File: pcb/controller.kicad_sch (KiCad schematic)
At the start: 3 parts, among them J1 Teensy 4.1 FEMALE 1x24, J2 Teensy 4.1 FEMALE 1x24, J3 VUSB from isolated Teensy pad

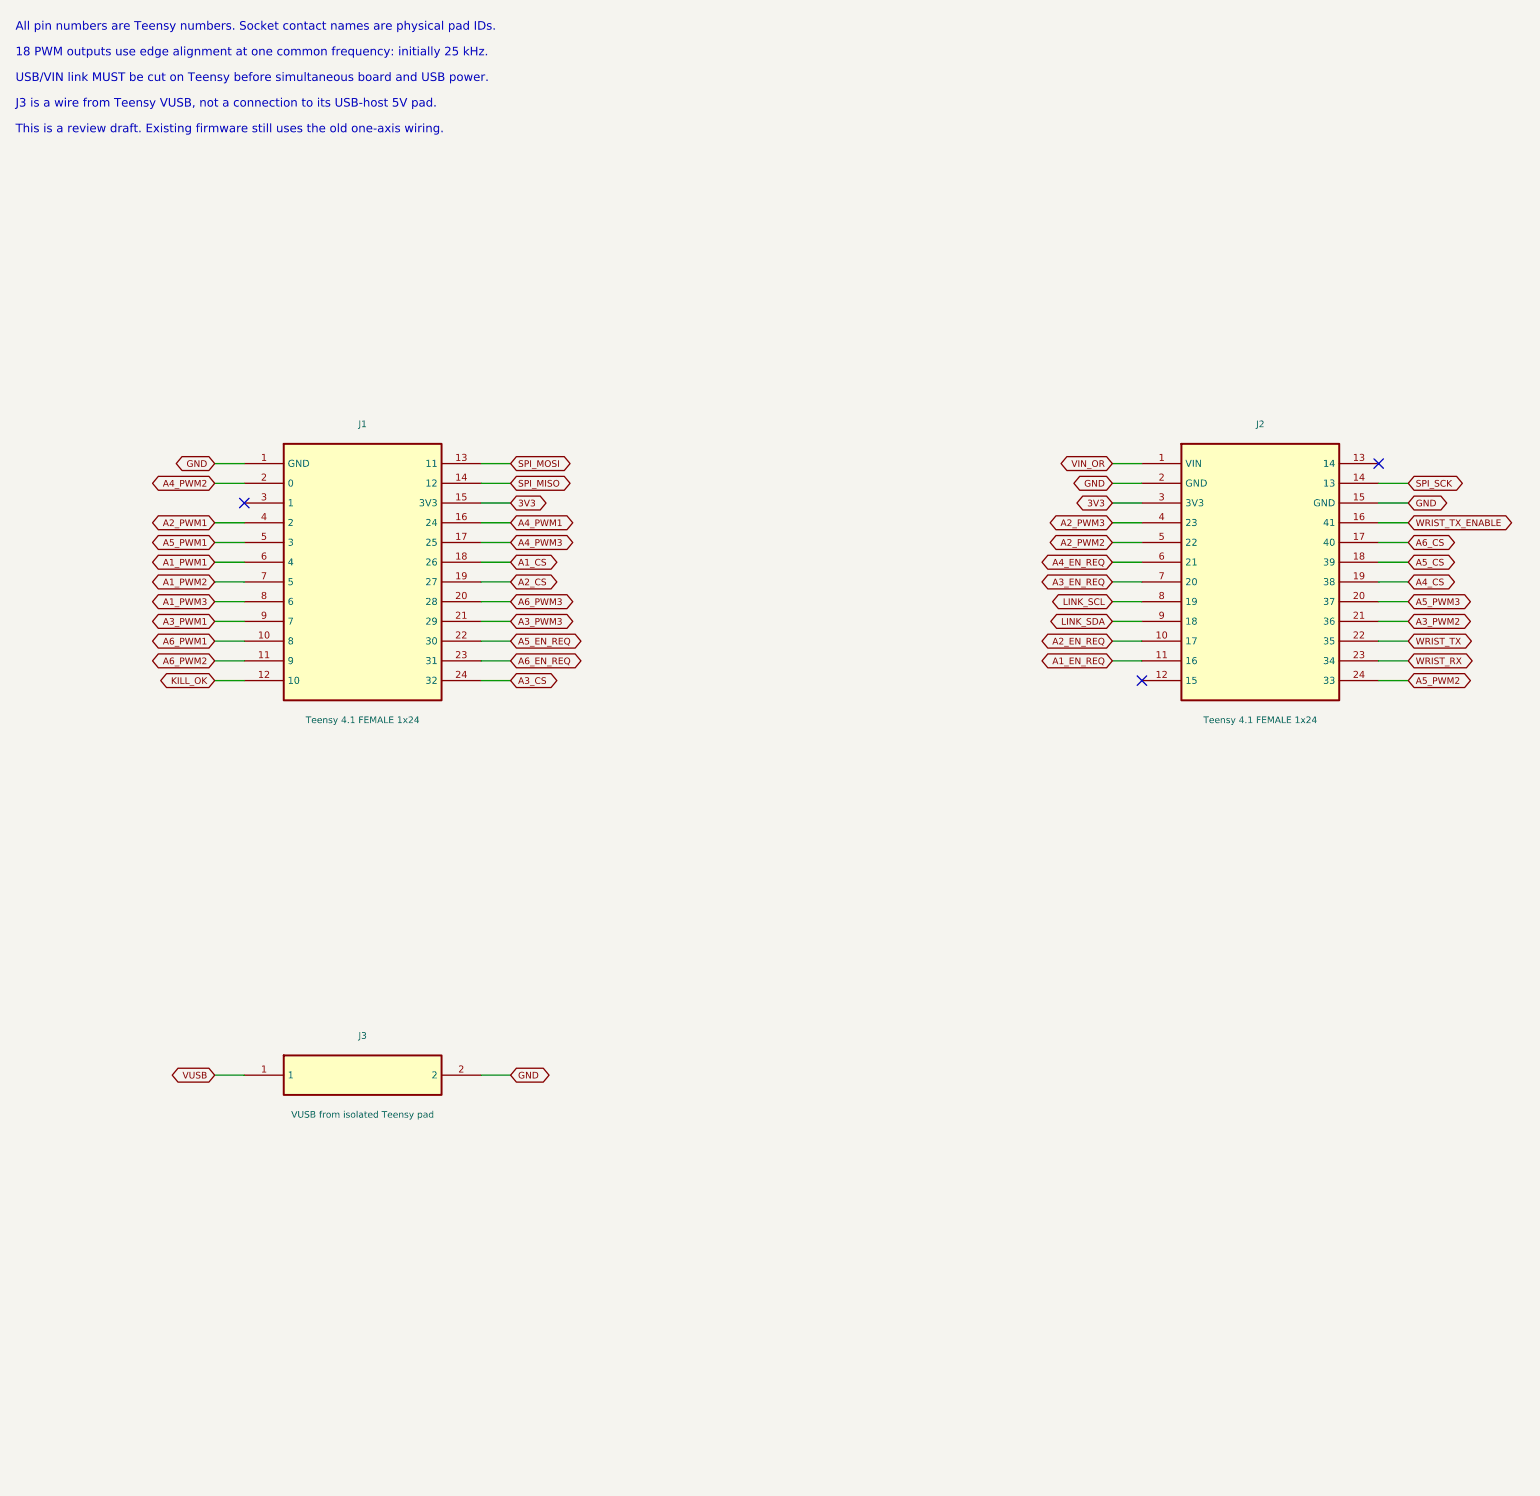
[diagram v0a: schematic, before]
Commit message: feat: finish through-hole six-axis carrier review design
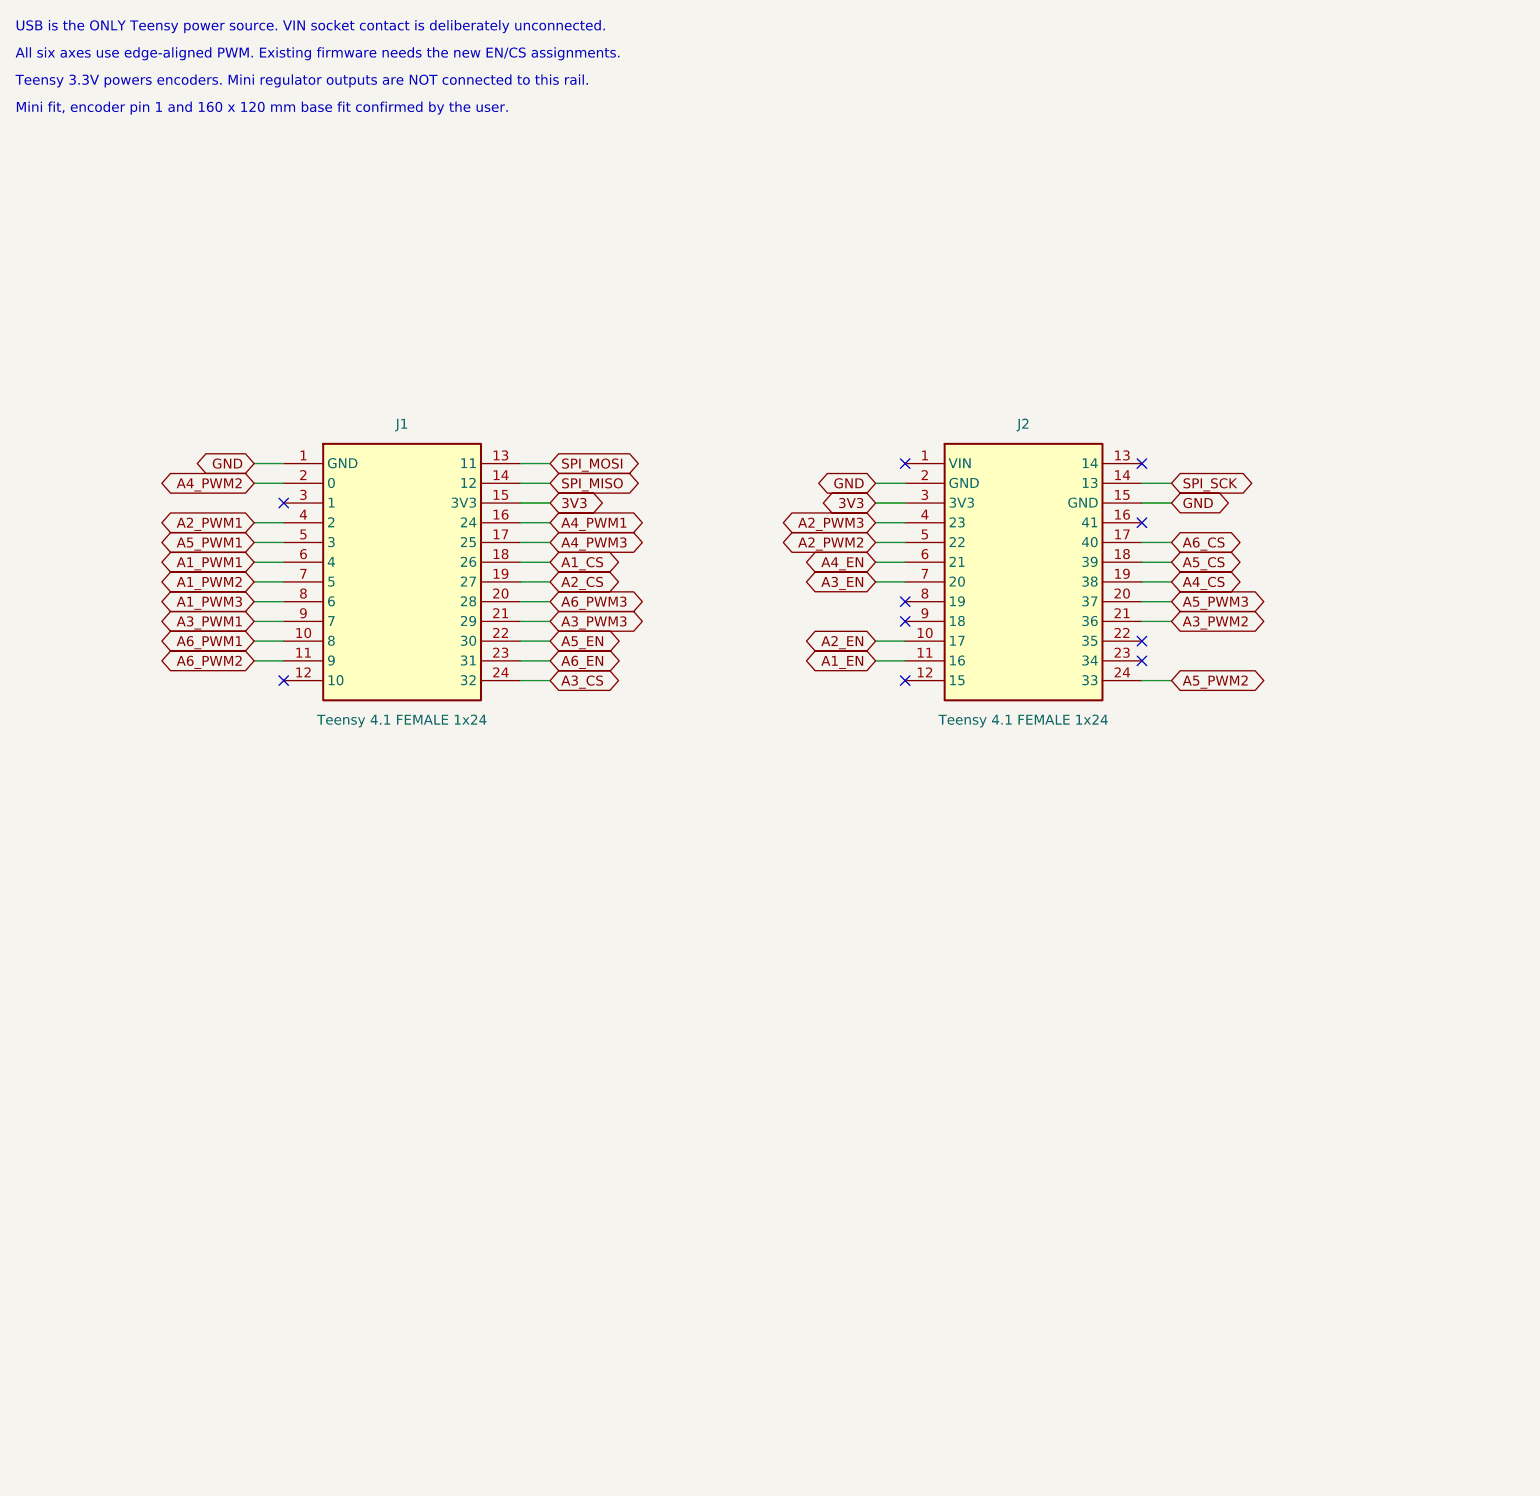
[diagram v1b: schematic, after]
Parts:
- removed J3: VUSB from isolated Teensy pad, Connector_PinHeader_2.54mm:PinHeader_1x02_P2.54mm_Vertical, symbol TrueSkate:J3
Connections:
- net A1_EN_REQ renamed A1_EN
- net A2_EN_REQ renamed A2_EN
- net A3_EN_REQ renamed A3_EN
- net A4_EN_REQ renamed A4_EN
- net A5_EN_REQ renamed A5_EN
- net A6_EN_REQ renamed A6_EN
- net KILL_OK: no longer names the net of J1.12 (10)
- net LINK_SCL: no longer names the net of J2.8 (19)
- net LINK_SDA: no longer names the net of J2.9 (18)
- net VIN_OR: no longer names the net of J2.1 (VIN)
- net WRIST_RX: no longer names the net of J2.23 (34)
- net WRIST_TX: no longer names the net of J2.22 (35)
- net WRIST_TX_ENABLE: no longer names the net of J2.16 (41)
- no-connect marks 3 -> 10
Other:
- note added: "All six axes use edge-aligned PWM. Existing firmware needs the new EN/CS assignments."
- note added: "Mini fit, encoder pin 1 and 160 x 120 mm base fit confirmed by the user."
- note added: "Teensy 3.3V powers encoders. Mini regulator outputs are NOT connected to this rail."
- note added: "USB is the ONLY Teensy power source. VIN socket contact is deliberately unconnected."
- note removed: "18 PWM outputs use edge alignment at one common frequency: initially 25 kHz."
- note removed: "All pin numbers are Teensy numbers. Socket contact names are physical pad IDs."
- note removed: "J3 is a wire from Teensy VUSB, not a connection to its USB-host 5V pad."
- note removed: "This is a review draft. Existing firmware still uses the old one-axis wiring."
- note removed: "USB/VIN link MUST be cut on Teensy before simultaneous board and USB power."
- title: 01 / Socketed Teensy and signal allocation -> 01 / USB-powered Teensy sockets
- moved on the sheet: J1, J2

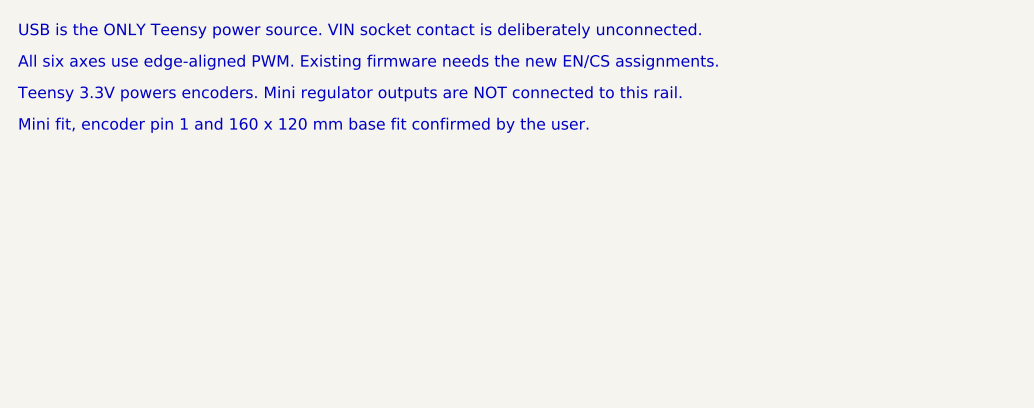
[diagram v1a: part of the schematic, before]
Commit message: feat: use exact Mini v1.0 footprints with direct power routing
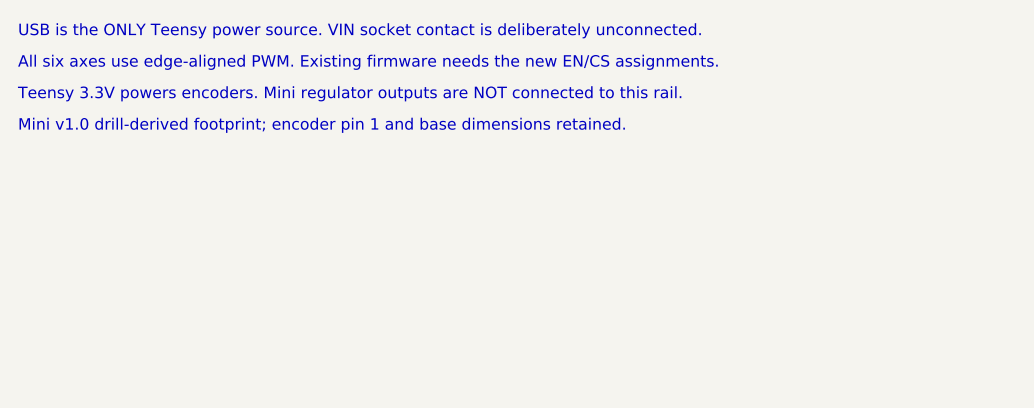
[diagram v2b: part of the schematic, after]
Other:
- note added: "Mini v1.0 drill-derived footprint; encoder pin 1 and base dimensions retained."
- note removed: "Mini fit, encoder pin 1 and 160 x 120 mm base fit confirmed by the user."
